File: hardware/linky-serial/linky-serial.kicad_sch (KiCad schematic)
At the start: 8 parts, among them J1 linky, J2 Conn_01x03_Pin, Q1 BSS123, U1 140814243000

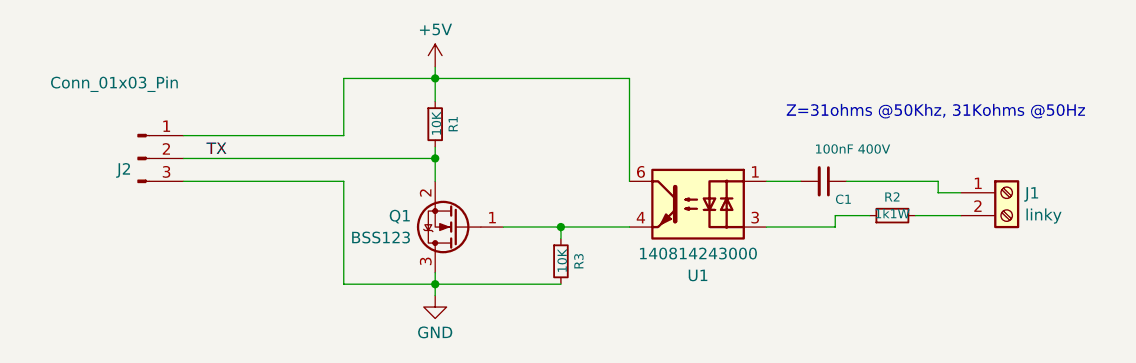
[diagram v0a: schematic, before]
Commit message: Fix transistor cabling (duh !)
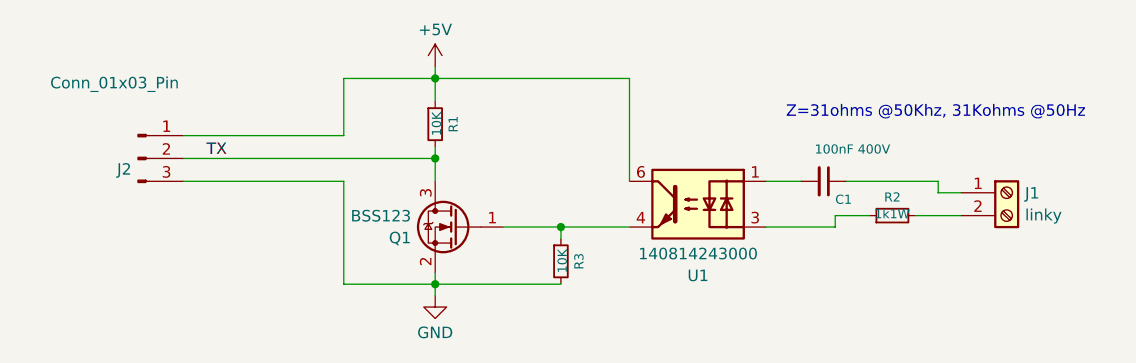
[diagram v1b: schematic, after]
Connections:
- net GND: now also Q1.2 (S); no longer Q1.3 (D)
- net TX: now also Q1.3 (D); no longer Q1.2 (S)
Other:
- moved on the sheet: Q1
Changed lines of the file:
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@@
 	(symbol
 		(lib_id "Transistor_FET:BSS123")
-		(at 110.49 111.76 180)
+		(at 110.49 111.76 0)
+		(mirror y)
 		(unit 1)
 		(exclude_from_sim no)
@@
 		(on_board yes)
 		(dnp no)
-		(fields_autoplaced yes)
 		(property "Reference" "Q1"
-			(at 105.2831 110.5478 0)
+			(at 105.2831 112.9722 0)
 			(effects
 				(font
@@
 		)
 		(property "Value" "BSS123"
-			(at 105.2831 112.9721 0)
+			(at 105.2831 110.5479 0)
 			(effects
 				(font
@@
 		)
 		(property "Footprint" "Package_TO_SOT_SMD:SOT-23"
-			(at 105.41 109.855 0)
+			(at 105.41 113.665 0)
 			(effects
 				(font
@@
 		)
 		(property "Datasheet" "http://www.diodes.com/assets/Datasheets/ds30366.pdf"
-			(at 105.41 107.95 0)
+			(at 105.41 115.57 0)
 			(effects
 				(font

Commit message: linky interface: update gate resitor value after tests
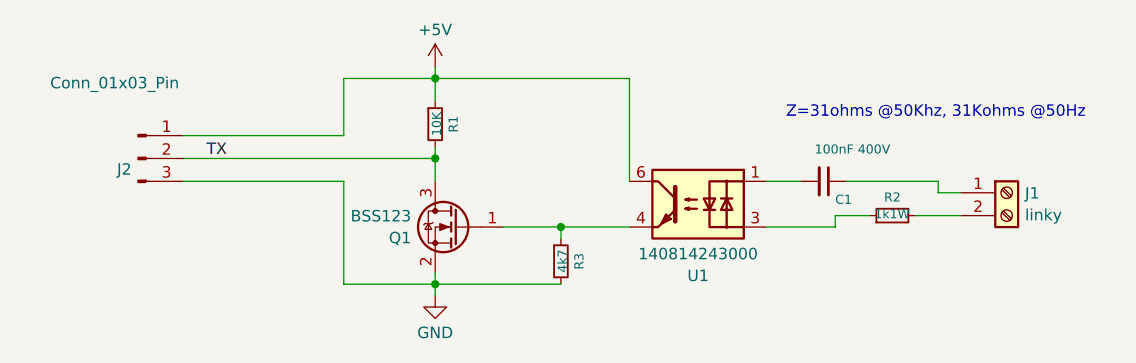
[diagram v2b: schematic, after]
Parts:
- R3: value 10K -> 4k7
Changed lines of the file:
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@@
 			)
 		)
-		(property "Value" "10K"
+		(property "Value" "4k7"
 			(at 122.0978 115.5446 90)
 			(effects
